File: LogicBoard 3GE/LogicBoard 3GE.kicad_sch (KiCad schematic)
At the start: 172 parts, among them IC103 LM386-3, IC201 2363, IC202 74LS00, IC203 74LS32, IC204 2114, IC205 2114, IC206 68A09, IC207 6522, IC208 AY3-8912, IC301 MC1408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

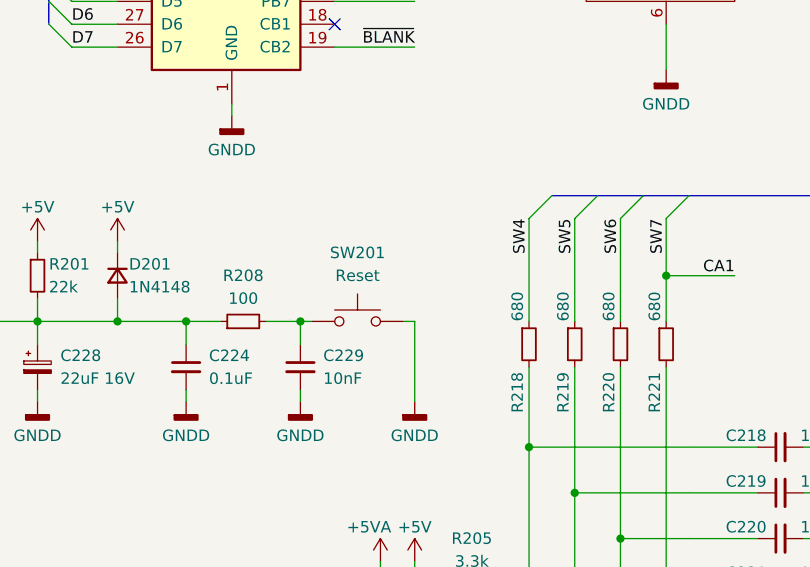
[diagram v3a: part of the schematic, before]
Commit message: fixed missing traces. fixed reset button connector. fixed some DRC warnings
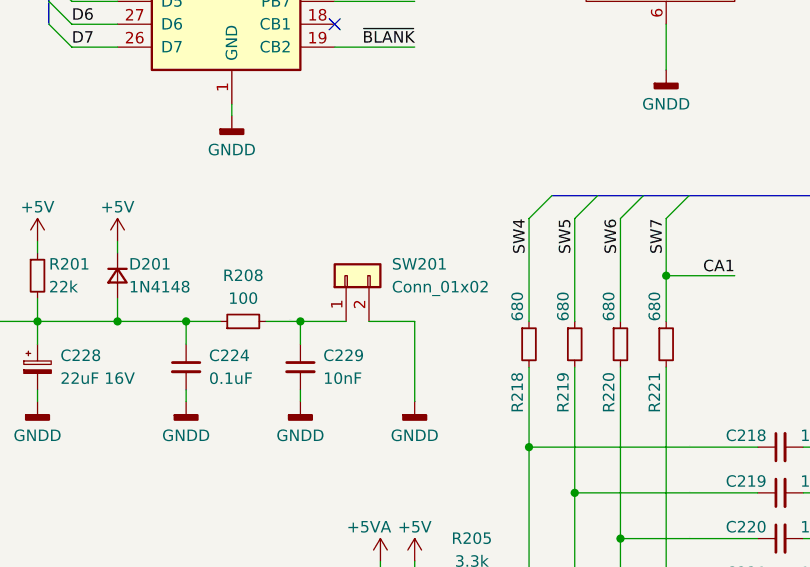
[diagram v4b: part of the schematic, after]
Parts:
- removed SW201: Reset, TestPoint:TestPoint_Bridge_Pitch5.08mm_Drill1.3mm, symbol Switch:SW_Push
- added SW201: Conn_01x02, Connector_JST:JST_EH_B2B-EH-A_1x02_P2.50mm_Vertical, symbol Connector_Generic:Conn_01x02
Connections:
- net GND: now also SW201.2 (Pin_2)
- net SWITCH_RESET: now also SW201.1 (Pin_1)
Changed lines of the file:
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@@
 	(wire
 		(pts
-			(xy 261.62 124.46) (xy 262.89 124.46)
+			(xy 261.62 124.46) (xy 266.7 124.46)
 		)
 		(stroke
@@
 	(wire
 		(pts
+			(xy 269.24 124.46) (xy 274.32 124.46)
+		)
+		(stroke
+			(width 0)
+			(type default)
+		)
+	)
+	(wire
+		(pts
 			(xy 138.43 237.49) (xy 137.16 237.49)
 		)
@@
 	(wire
 		(pts
-			(xy 273.05 124.46) (xy 274.32 124.46)
-		)
-		(stroke
-			(width 0)
-			(type default)
-		)
-	)
-	(wire
-		(pts
 			(xy 280.67 181.61) (xy 304.8 181.61)
 		)
@@
 	)
 	(symbol
-		(lib_id "Switch:SW_Push")
-		(at 267.97 124.46 0)
-		(unit 1)
-		(exclude_from_sim no)
-		(in_bom yes)
-		(on_board yes)
-		(dnp no)
-		(property "Reference" "SW201"
-			(at 267.97 116.84 0)
-			(effects
-				(font
-					(size 1.27 1.27)
-				)
-			)
-		)
-		(property "Value" "Reset"
-			(at 267.97 119.38 0)
-			(effects
-				(font
-					(size 1.27 1.27)
-				)
-			)
-		)
-		(property "Footprint" "TestPoint:TestPoint_Bridge_Pitch5.08mm_Drill1.3mm"
-			(at 267.97 119.38 0)
-			(effects
-				(font
-					(size 1.27 1.27)
-				)
-				(hide yes)
-			)
-		)
-		(property "Datasheet" "~"
-			(at 267.97 119.38 0)
-			(effects
-				(font
-					(size 1.27 1.27)
-				)
-				(hide yes)
-			)
-		)
-		(property "Description" ""
-			(at 267.97 124.46 0)
-			(effects
-				(font
-					(size 1.27 1.27)
-				)
-				(hide yes)
-			)
-		)
-		(pin "1"
-		)
-		(pin "2"
-		)
-		(instances
-			(project ""
-				(path "/e63e39d7-6ac0-4ffd-8aa3-1841a4541b55"
-					(reference "SW201")
-					(unit 1)
-				)
-			)
-		)
-	)
-	(symbol
 		(lib_id "Device:C_Small")
 		(at 377.19 177.8 0)
@@
 					(unit 1)
 				)
+			)
+		)
+	)
+	(symbol
+		(lib_id "Connector_Generic:Conn_01x02")
+		(at 266.7 119.38 90)
+		(unit 1)
+		(exclude_from_sim no)
+		(in_bom yes)
+		(on_board yes)
+		(dnp no)
+		(fields_autoplaced yes)
+		(property "Reference" "SW201"
+			(at 271.78 118.1099 90)
+			(effects
+				(font
+					(size 1.27 1.27)
+				)
+				(justify right)
+			)
+		)
+		(property "Value" "Conn_01x02"
+			(at 271.78 120.6499 90)
+			(effects
+				(font
+					(size 1.27 1.27)
+				)
+				(justify right)
+			)
+		)
+		(property "Footprint" "Connector_JST:JST_EH_B2B-EH-A_1x02_P2.50mm_Vertical"
+			(at 266.7 119.38 0)
+			(effects
+				(font
+					(size 1.27 1.27)
+				)
+				(hide yes)
+			)
+		)
+		(property "Datasheet" "~"
+			(at 266.7 119.38 0)
+			(effects
+				(font
+					(size 1.27 1.27)
+				)
+				(hide yes)
+			)
+		)
+		(property "Description" "Generic connector, single row, 01x02, script generated (kicad-library-utils/schlib/autogen/connector/)"
+			(at 266.7 119.38 0)
+			(effects
+				(font
+					(size 1.27 1.27)
+				)
+				(hide yes)
+			)
+		)
+		(pin "1"
+		)
+		(pin "2"
+		)
+		(instances
+			(project ""
+				(path "/e63e39d7-6ac0-4ffd-8aa3-1841a4541b55"
+					(reference "SW201")
+					(unit 1)
+				)

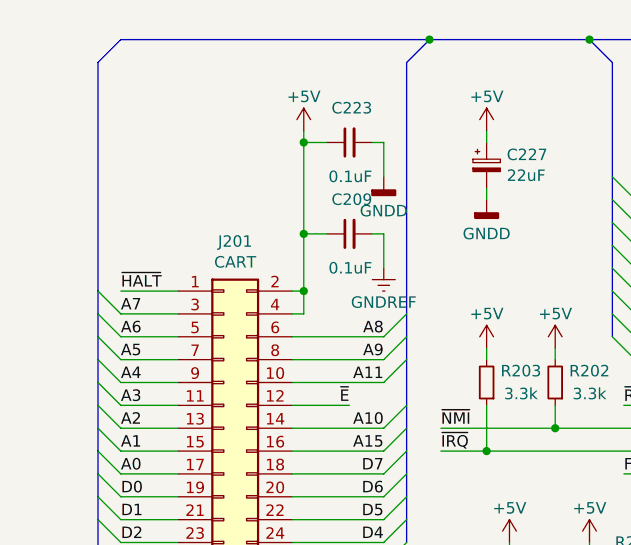
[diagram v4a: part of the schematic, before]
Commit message: update cart connector to AMP 5645384-1 with 3D model
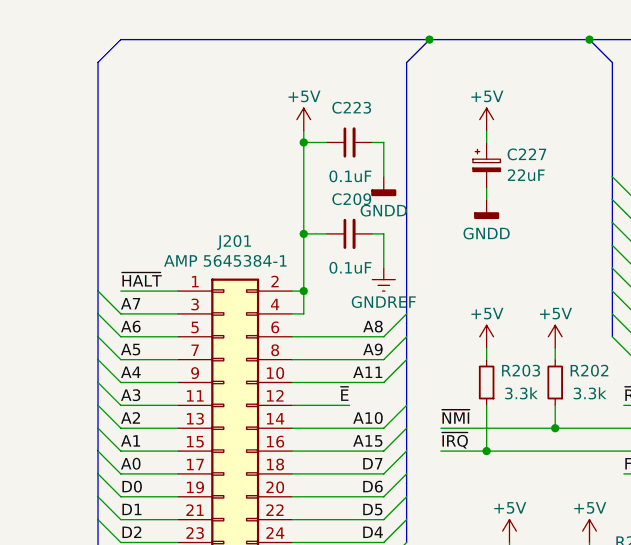
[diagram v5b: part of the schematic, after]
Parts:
- J201: value CART -> AMP 5645384-1
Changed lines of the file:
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@@
 			)
 		)
-		(property "Value" "CART"
-			(at 39.37 45.0596 0)
+		(property "Value" "AMP 5645384-1"
+			(at 38.354 44.958 0)
 			(effects
 				(font
